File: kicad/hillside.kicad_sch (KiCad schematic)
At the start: 65 parts, among them J1 Haptic, J2 TRRS, J3 Bat_Pos, J4 Bat_GND, K1 SW_Key, K10 SW_Key, K11 SW_Key, K12 SW_Key, K13 SW_Key, K14 SW_Key, K15 SW_Key, K16 SW_Key, K17 SW_Key, K18 SW_Key, K19 SW_Key, K2 SW_Key, K20 SW_Rotary, K21 SW_Key, K22 SW_Key, K23 SW_Key, K24 SW_Key, K3 SW_Key, K4 SW_Key, K5 SW_Key, K6 SW_Key, K7 SW_Key, K8 SW_Key, K9 SW_Key, SW1 Reset, SW2 SW_Power, U1 ProMicro_r

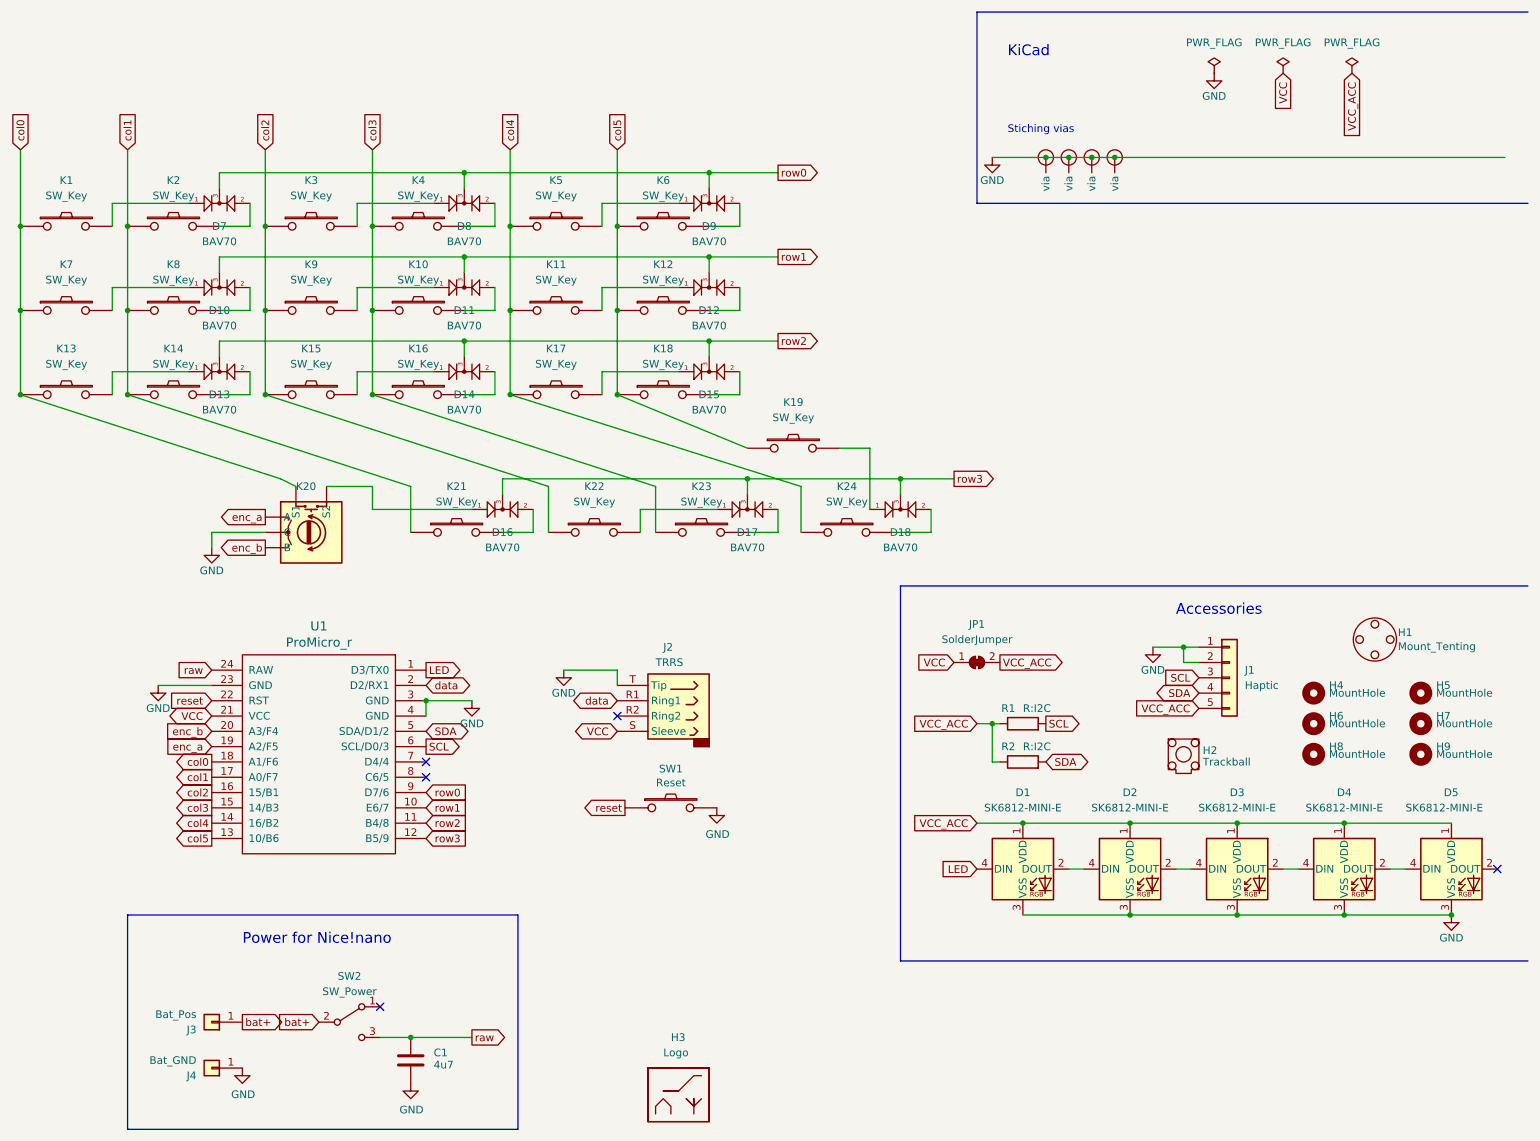
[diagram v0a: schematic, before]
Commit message: Remove project copies of standard lib symbols
- R, C, Jumper, MountingHole, GND, PowerFlag,
- Conn_01x01, Conn_01x05, SW_SPDT
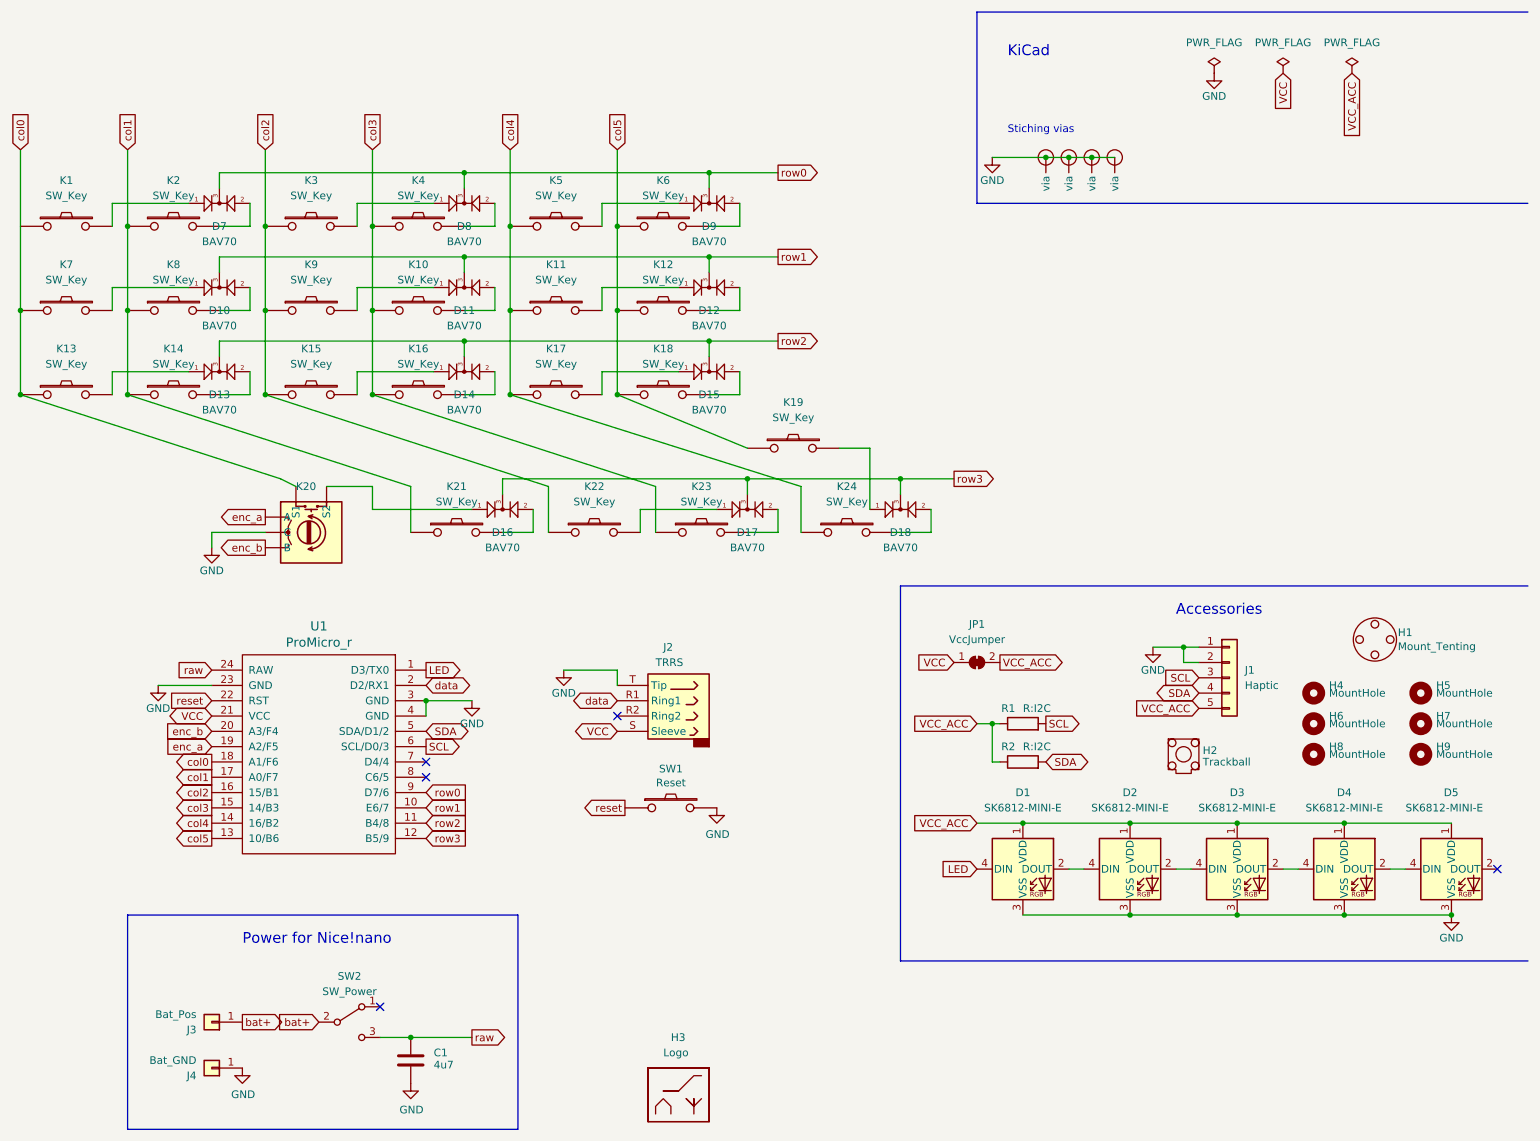
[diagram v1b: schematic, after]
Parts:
- C1: symbol hillside_basic:C -> Device:C
- H4, H5, H6, H7, H8, H9: symbol hillside_basic:MountingHole -> Mechanical:MountingHole
- J1: symbol hillside_basic:Conn_01x05-Connector_Generic -> Connector_Generic:Conn_01x05
- J3, J4: symbol hillside_basic:Conn_01x01 -> Connector_Generic:Conn_01x01
- JP1: value SolderJumper -> VccJumper; symbol hillside_basic:SolderJumper_2_Bridged -> Jumper:SolderJumper_2_Bridged
- R1, R2: symbol hillside_basic:R -> Device:R
- SW2: symbol hillside_basic:SW_SPDT -> Switch:SW_SPDT
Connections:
- net col0: no longer K1.1
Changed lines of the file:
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@@
   (junction (at 130.81 53.34) (diameter 0) (color 0 0 0 0)
   )
-  (junction (at 198.12 36.83) (diameter 0) (color 0 0 0 0)
-  )
   (junction (at 115.57 48.26) (diameter 0) (color 0 0 0 0)
   )
@@
   )
   (junction (at 186.69 36.83) (diameter 0) (color 0 0 0 0)
-  )
-  (junction (at 16.51 48.26) (diameter 0) (color 0 0 0 0)
   )
   (junction (at 218.44 162.56) (diameter 0) (color 0 0 0 0)
@@
     (stroke (width 0) (type default) (color 0 0 0 0))
   )
-  (wire (pts (xy 198.12 36.83) (xy 262.89 36.83))
-    (stroke (width 0) (type default) (color 0 0 0 0))
-  )
   (wire (pts (xy 113.03 58.42) (xy 125.73 58.42))
     (stroke (width 0) (type default) (color 0 0 0 0))
@@
     (stroke (width 0) (type default) (color 0 0 0 0))
   )
-  (wire (pts (xy 16.51 35.56) (xy 16.51 48.26))
-    (stroke (width 0) (type default) (color 0 0 0 0))
-  )
   (wire (pts (xy 90.17 69.85) (xy 90.17 67.31))
     (stroke (width 0) (type default) (color 0 0 0 0))
@@
     (stroke (width 0) (type default) (color 0 0 0 0))
   )
-  (wire (pts (xy 16.51 48.26) (xy 16.51 62.23))
+  (wire (pts (xy 16.51 35.56) (xy 16.51 62.23))
     (stroke (width 0) (type default) (color 0 0 0 0))
   )
@@
     (pin "2")
   )
-  (symbol (lib_id "hillside_basic:GND") (at 132.08 144.78 0) (unit 1)
+  (symbol (lib_id "power:GND") (at 132.08 144.78 0) (unit 1)
     (in_bom yes) (on_board yes)
     (property "Reference" "#PWR04" (id 0) (at 132.08 151.13 0)
@@
     (pin "4")
   )
-  (symbol (lib_id "hillside_basic:GND") (at 214.63 22.86 0) (unit 1)
+  (symbol (lib_id "power:GND") (at 214.63 22.86 0) (unit 1)
     (in_bom yes) (on_board yes)
     (property "Reference" "#PWR06" (id 0) (at 214.63 29.21 0)
@@
     (pin "1")
   )
-  (symbol (lib_id "hillside_basic:GND") (at 254 162.56 0) (unit 1)
+  (symbol (lib_id "power:GND") (at 254 162.56 0) (unit 1)
     (in_bom yes) (on_board yes)
     (property "Reference" "#PWR05" (id 0) (at 254 168.91 0)
@@
     (pin "S2")
   )
-  (symbol (lib_id "hillside_basic:GND") (at 48.26 101.6 0) (unit 1)
+  (symbol (lib_id "power:GND") (at 48.26 101.6 0) (unit 1)
     (in_bom yes) (on_board yes)
     (property "Reference" "#PWR0101" (id 0) (at 48.26 107.95 0)
@@
     (pin "1")
   )
-  (symbol (lib_id "hillside_basic:GND") (at 177.8 36.83 0) (unit 1)
+  (symbol (lib_id "power:GND") (at 177.8 36.83 0) (unit 1)
     (in_bom yes) (on_board yes)
     (property "Reference" "#PWR0102" (id 0) (at 177.8 43.18 0)
@@
     (pin "9")
   )
-  (symbol (lib_id "hillside_basic:Conn_01x05-Connector_Generic") (at 217.17 123.19 0) (unit 1)
+  (symbol (lib_id "Connector_Generic:Conn_01x05") (at 217.17 123.19 0) (unit 1)
     (in_bom yes) (on_board yes)
     (property "Reference" "J1" (id 0) (at 219.71 121.92 0)
@@
     (pin "2")
   )
-  (symbol (lib_id "hillside_basic:PWR_FLAG") (at 214.63 22.86 0) (unit 1)
+  (symbol (lib_id "power:PWR_FLAG") (at 214.63 22.86 0) (unit 1)
     (in_bom yes) (on_board yes)
     (property "Reference" "#FLG02" (id 0) (at 214.63 20.955 0)
@@
     (pin "1")
   )
-  (symbol (lib_id "hillside_basic:PWR_FLAG") (at 226.06 22.86 0) (unit 1)
+  (symbol (lib_id "power:PWR_FLAG") (at 226.06 22.86 0) (unit 1)
     (in_bom yes) (on_board yes)
     (property "Reference" "#FLG01" (id 0) (at 226.06 20.955 0)
@@
     (pin "1")
   )
-  (symbol (lib_id "hillside_basic:R") (at 182.88 130.81 90) (unit 1)
+  (symbol (lib_id "Device:R") (at 182.88 130.81 90) (unit 1)
     (in_bom yes) (on_board yes)
     (property "Reference" "R1" (id 0) (at 181.61 128.27 90)
@@
     (pin "2")
   )
-  (symbol (lib_id "hillside_basic:R") (at 182.88 137.16 90) (unit 1)
+  (symbol (lib_id "Device:R") (at 182.88 137.16 90) (unit 1)
     (in_bom yes) (on_board yes)
     (property "Reference" "R2" (id 0) (at 181.61 134.62 90)
@@
     (pin "2")
   )
-  (symbol (lib_id "hillside_basic:GND") (at 39.37 124.46 0) (unit 1)
+  (symbol (lib_id "power:GND") (at 39.37 124.46 0) (unit 1)
     (in_bom yes) (on_board yes)
     (property "Reference" "#PWR02" (id 0) (at 39.37 130.81 0)
@@
     (pin "3")
   )
-  (symbol (lib_id "hillside_basic:Conn_01x01") (at 48.26 180.34 180) (unit 1)
+  (symbol (lib_id "Connector_Generic:Conn_01x01") (at 48.26 180.34 180) (unit 1)
     (in_bom yes) (on_board yes)
     (property "Reference" "J3" (id 0) (at 45.72 181.61 0)
@@
     (pin "1")
   )
-  (symbol (lib_id "hillside_basic:Conn_01x01") (at 48.26 187.96 180) (unit 1)
+  (symbol (lib_id "Connector_Generic:Conn_01x01") (at 48.26 187.96 180) (unit 1)
     (in_bom yes) (on_board yes)
     (property "Reference" "J4" (id 0) (at 45.72 189.23 0)
@@
     (pin "1")
   )
-  (symbol (lib_id "hillside_basic:GND") (at 53.34 187.96 0) (unit 1)
+  (symbol (lib_id "power:GND") (at 53.34 187.96 0) (unit 1)
     (in_bom yes) (on_board yes)
     (property "Reference" "#PWR01" (id 0) (at 53.34 194.31 0)
@@
     (pin "1")
   )
-  (symbol (lib_id "hillside_basic:SW_SPDT") (at 71.12 180.34 0) (unit 1)
+  (symbol (lib_id "Switch:SW_SPDT") (at 71.12 180.34 0) (unit 1)
     (in_bom yes) (on_board yes)
     (property "Reference" "SW2" (id 0) (at 71.12 172.72 0))
@@
     (pin "T")
   )
-  (symbol (lib_id "hillside_basic:GND") (at 106.68 121.92 0) (unit 1)
+  (symbol (lib_id "power:GND") (at 106.68 121.92 0) (unit 1)
     (in_bom yes) (on_board yes)
     (property "Reference" "#PWR09" (id 0) (at 106.68 128.27 0)
@@
     (pin "1")
   )
-  (symbol (lib_id "hillside_basic:SolderJumper_2_Bridged") (at 175.26 120.65 0) (unit 1)
+  (symbol (lib_id "Jumper:SolderJumper_2_Bridged") (at 175.26 120.65 0) (unit 1)
     (in_bom yes) (on_board yes)
     (property "Reference" "JP1" (id 0) (at 175.26 114.3 0))
-    (property "Value" "SolderJumper" (id 1) (at 175.26 116.84 0))
+    (property "Value" "VccJumper" (id 1) (at 175.26 116.84 0))
     (property "Footprint" "Jumper:SolderJumper-2_P1.3mm_Bridged_RoundedPad1.0x1.5mm" (id 2) (at 175.26 120.65 0)
       (effects (font (size 1.27 1.27)) hide)
@@
     (pin "2")
   )
-  (symbol (lib_id "hillside_basic:PWR_FLAG") (at 237.49 22.86 0) (unit 1)
+  (symbol (lib_id "power:PWR_FLAG") (at 237.49 22.86 0) (unit 1)
     (in_bom yes) (on_board yes)
     (property "Reference" "#FLG0101" (id 0) (at 237.49 20.955 0)
@@
     (pin "1")
   )
-  (symbol (lib_id "hillside_basic:GND") (at 91.44 127 0) (unit 1)
+  (symbol (lib_id "power:GND") (at 91.44 127 0) (unit 1)
     (in_bom yes) (on_board yes)
     (property "Reference" "#PWR0103" (id 0) (at 91.44 133.35 0)
@@
     (pin "1")
   )
-  (symbol (lib_id "hillside_basic:GND") (at 204.47 118.11 0) (unit 1)
+  (symbol (lib_id "power:GND") (at 204.47 118.11 0) (unit 1)
     (in_bom yes) (on_board yes)
     (property "Reference" "#PWR0104" (id 0) (at 204.47 124.46 0)
@@
     (pin "1")
   )
-  (symbol (lib_id "hillside_basic:GND") (at 81.28 190.5 0) (unit 1)
+  (symbol (lib_id "power:GND") (at 81.28 190.5 0) (unit 1)
     (in_bom yes) (on_board yes)
     (property "Reference" "#PWR08" (id 0) (at 81.28 196.85 0)
@@
     (pin "1")
   )
-  (symbol (lib_id "hillside_basic:C") (at 81.28 186.69 0) (unit 1)
+  (symbol (lib_id "Device:C") (at 81.28 186.69 0) (unit 1)
     (in_bom yes) (on_board yes)
     (property "Reference" "C1" (id 0) (at 85.09 185.42 0)
@@
     )
   )
-  (symbol (lib_id "hillside_basic:MountingHole") (at 248.92 125.73 0) (unit 1)
+  (symbol (lib_id "Mechanical:MountingHole") (at 248.92 125.73 0) (unit 1)
     (in_bom yes) (on_board yes)
     (property "Reference" "H5" (id 0) (at 251.46 124.46 0)
@@
     )
   )
-  (symbol (lib_id "hillside_basic:MountingHole") (at 248.92 130.81 0) (unit 1)
+  (symbol (lib_id "Mechanical:MountingHole") (at 248.92 130.81 0) (unit 1)
     (in_bom yes) (on_board yes)
     (property "Reference" "H7" (id 0) (at 251.46 129.54 0)
@@
     )
   )
-  (symbol (lib_id "hillside_basic:MountingHole") (at 231.14 125.73 0) (unit 1)
+  (symbol (lib_id "Mechanical:MountingHole") (at 231.14 125.73 0) (unit 1)
     (in_bom yes) (on_board yes)
     (property "Reference" "H4" (id 0) (at 233.68 124.46 0)
@@
     )
   )
-  (symbol (lib_id "hillside_basic:MountingHole") (at 231.14 130.81 0) (unit 1)
+  (symbol (lib_id "Mechanical:MountingHole") (at 231.14 130.81 0) (unit 1)
     (in_bom yes) (on_board yes)
     (property "Reference" "H6" (id 0) (at 233.68 129.54 0)
@@
     )
   )
-  (symbol (lib_id "hillside_basic:MountingHole") (at 231.14 135.89 0) (unit 1)
+  (symbol (lib_id "Mechanical:MountingHole") (at 231.14 135.89 0) (unit 1)
     (in_bom yes) (on_board yes)
     (property "Reference" "H8" (id 0) (at 233.68 134.62 0)
@@
     )
   )
-  (symbol (lib_id "hillside_basic:MountingHole") (at 248.92 135.89 0) (unit 1)
+  (symbol (lib_id "Mechanical:MountingHole") (at 248.92 135.89 0) (unit 1)
     (in_bom yes) (on_board yes)
     (property "Reference" "H9" (id 0) (at 251.46 134.62 0)
@@
     )
     (path "/00000000-0000-0000-0000-000061a8564f"
-      (reference "JP1") (unit 1) (value "SolderJumper") (footprint "Jumper:SolderJumper-2_P1.3mm_Bridged_RoundedPad1.0x1.5mm")
+      (reference "JP1") (unit 1) (value "VccJumper") (footprint "Jumper:SolderJumper-2_P1.3mm_Bridged_RoundedPad1.0x1.5mm")
     )
     (path "/00000000-0000-0000-0000-0000617cbce8"
